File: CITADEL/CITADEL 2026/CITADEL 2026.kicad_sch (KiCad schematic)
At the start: 33 parts, among them J1 Vibration Motor, J2 Linear Actuator, U3 TJA1051T-3

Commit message: Updated Schematic
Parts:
- removed A1, A2: Pololu_Breakout_DRV8825, Module:Pololu_Breakout-16_15.2x20.3mm, symbol Driver_Motor:Pololu_Breakout_DRV8825
- added J18: CAN BUS, Connector_AMASS:AMASS_XT30U-F_1x02_P5.0mm_Vertical, symbol Connector:Conn_01x02_Pin
- added J19: Battery Connections, Connector_AMASS:AMASS_XT60-M_1x02_P7.20mm_Vertical, symbol Connector:Conn_01x02_Pin
- added J3: LED Strip, Connector_JST:JST_EH_B3B-EH-A_1x03_P2.50mm_Vertical, symbol Connector:Conn_01x03_Pin
- added J4: Spark Max, Connector_JST:JST_EH_B2B-EH-A_1x02_P2.50mm_Vertical, symbol Connector:Conn_01x02_Pin
- added P1: PS1, Citadel:D24V15OF5, symbol Citadel-altium-import:root_2_Pololu_5V,_15A_Step-Down_Voltage_Regulator_D24V150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
- added P2: PS2, Citadel:D24V15OF5, symbol Citadel-altium-import:root_0_Pololu_12V,_15A_Step-Down_Voltage_Regulator_D24V15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
- added Q7: SSM3K329R_LF, Citadel:SSM3K329_LF, symbol Citadel-altium-import:root_0_SSM3K329R_LF
- added U1: VNH7070ASTR, Jayse_Footprints:SO_0ASTR_STM, symbol 2026-01-09_23-32-14:VNH7070ASTR
- MG90S1, MG90S2, MG90S3, MG90S4, MG90S5, MG90S6, MG90S7, MG90S8, MG90S9: footprint (none) -> Connector_Molex:Molex_Mini-Fit_Jr_5566-04A_2x02_P4.20mm_Vertical
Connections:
- net Vibration_Motor_1 is gone; now on net +12V: J1.2 (Pin_2)
- net +12V: now also J3.1 (Pin_1), P2.VOUT, P2.VOUT_1 (VOUT), P2.VOUT_2 (VOUT)
- net +5V: now also P1.VOUT, P1.VOUT_1 (VOUT), P1.VOUT_2 (VOUT)
- net +BATT: now also J19.2 (Pin_2), P1.VIN, P1.VIN_1 (VIN), P1.VIN_2 (VIN), P2.VIN, P2.VIN_1 (VIN), P2.VIN_2 (VIN), U1.12 (VCC), U1.4 (VCC), U1.5 (VCC)
- net CIT_CAN+: now also J18.2 (Pin_2)
- net CIT_CAN-: now also J18.1 (Pin_1)
- net CRX_ESP: now also U2.12 (GPIO12/A15); no longer U2.11 (GPIO14/A16)
- net GND: now also J19.1 (Pin_1), J3.3 (Pin_3), J4.2 (Pin_2), P1.GND, P1.GND1 (GND), P1.GND2 (GND), P1.GND3 (GND), P1.GND4 (GND), P1.GND5 (GND), P1.GND6 (GND), P1.GND7 (GND), P2.GND, P2.GND1 (GND), P2.GND2 (GND), P2.GND3 (GND), P2.GND4 (GND), P2.GND5 (GND), P2.GND6 (GND), P2.GND7 (GND), Q7.2, U1.1 (GNDA), U1.16 (GNDA), U1.8 (GNDB), U1.9 (GNDB)
- net MG90S1: now also U2.30 (GPIO23/MOSI); no longer U2.9 (GPIO26/A19)
- net MG90S2: now also U2.29 (GPIO22/SCL); no longer U2.12 (GPIO12/A15)
- net MG90S3: now also U2.28 (GPIO1/TX0); no longer U2.30 (GPIO23/MOSI)
- net MG90S4: now also U2.27 (GPIO3/RX0); no longer U2.29 (GPIO22/SCL)
- net MG90S5: now also U2.26 (GPIO21/SDA); no longer U2.28 (GPIO1/TX0)
- net MG90S6: now also U2.25 (GPIO19/MISO); no longer U2.27 (GPIO3/RX0)
- net MG90S7: now also U2.24 (GPIO18/SCK); no longer U2.26 (GPIO21/SDA)
- net MG90S8: now also U2.23 (GPIO05/CS); no longer U2.25 (GPIO19/MISO)
- net MG90S9: now also U2.22 (GPIO17/TX2); no longer U2.24 (GPIO18/SCK)
- net DIR renamed Actuator_INA
- net Actuator_INA: now also U1.3 (INA)
- net Linear_Actuator_1 renamed Lin_Actuator_A
- net Lin_Actuator_A: now also U1.15 (OUTA), U1.2 (OUTA)
- net Linear_Actuator_2 renamed Lin_Actuator_B
- net Lin_Actuator_B: now also U1.10 (OUTB), U1.7 (OUTB)
- net Linear_Actuator_STEP renamed VibMotorSignal
- net VibMotorSignal: now also Q7.1
- net Step_Motor_Enable renamed LED_Strip
- net LED_Strip: now also J3.2 (Pin_2)
- net Vibration_Motor_2 renamed VibMotorMOS
- net VibMotorMOS: now also Q7.3
- net Vibration_Motor_STEP renamed Actuator_INB
- net Actuator_INB: now also U1.6 (INB)
- new net Actuator_PWM: U1.11 (PWM), U2.9 (GPIO26/A19)
- new net Spark_Max_PWM: J4.1 (Pin_1), U2.11 (GPIO14/A16)
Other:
- note added: "CAN Transceiver"
- note added: "Communication and Power"
- note added: "LED Strip"
- note added: "MCU"
- note added: "Power Regulators"
- moved on the sheet: C1, C2, C3, D4, J1, J2, JP1, MG90S1, MG90S2, MG90S3, MG90S4, MG90S5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

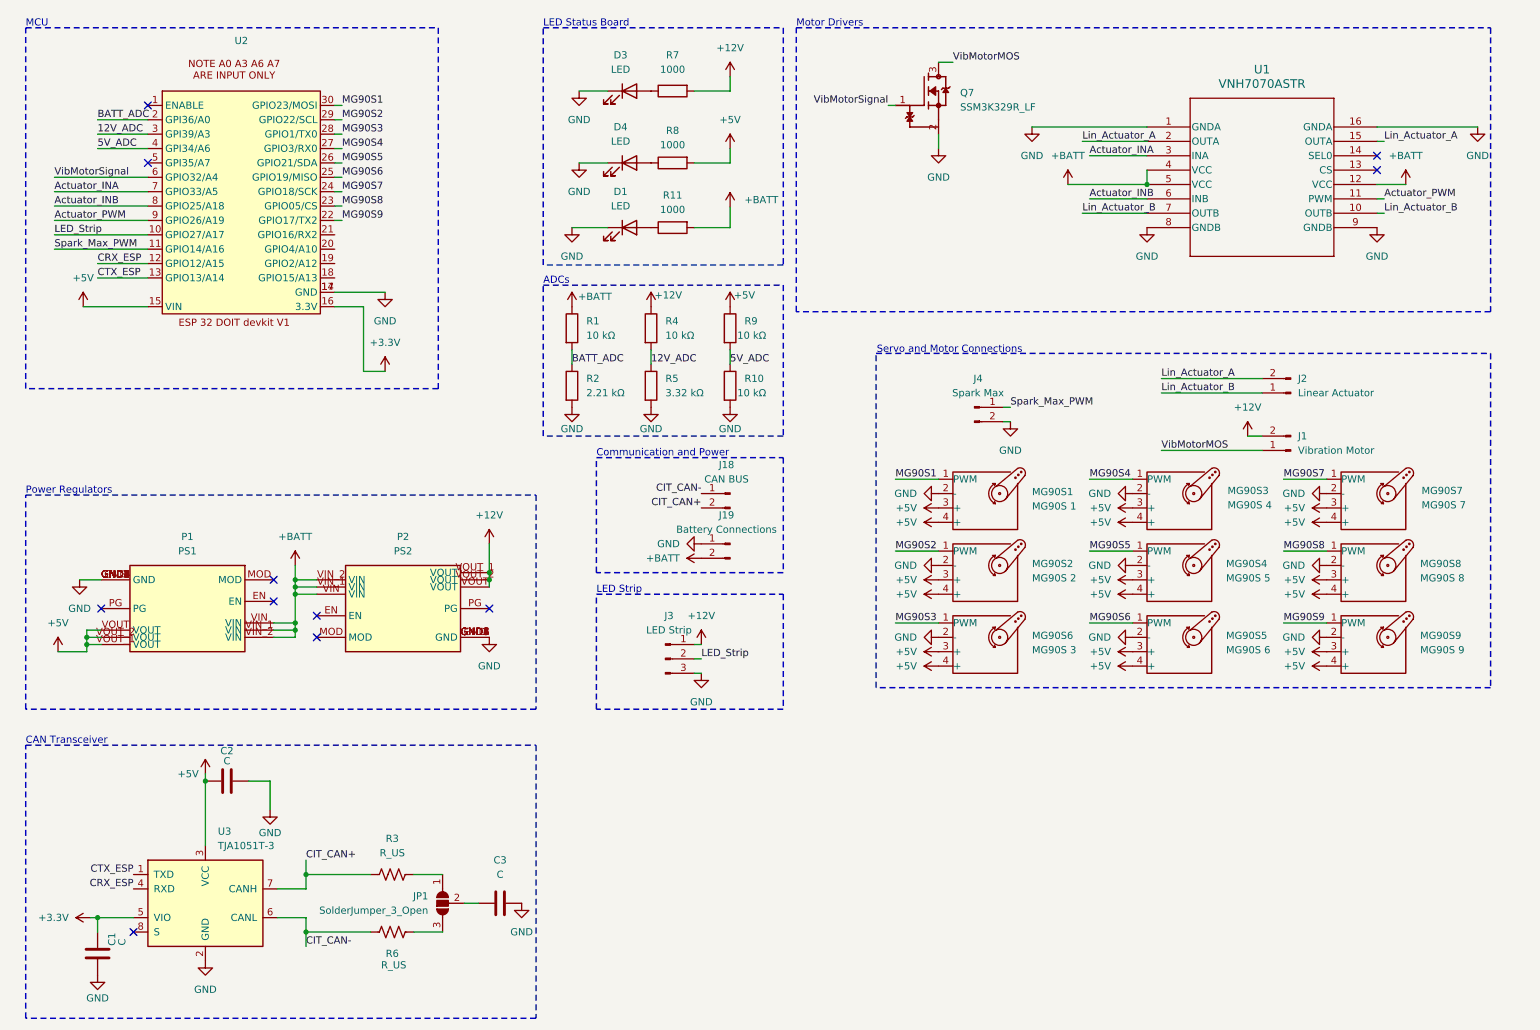
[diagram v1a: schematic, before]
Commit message: Updated Schematic
Changed MCU, added additional connectors
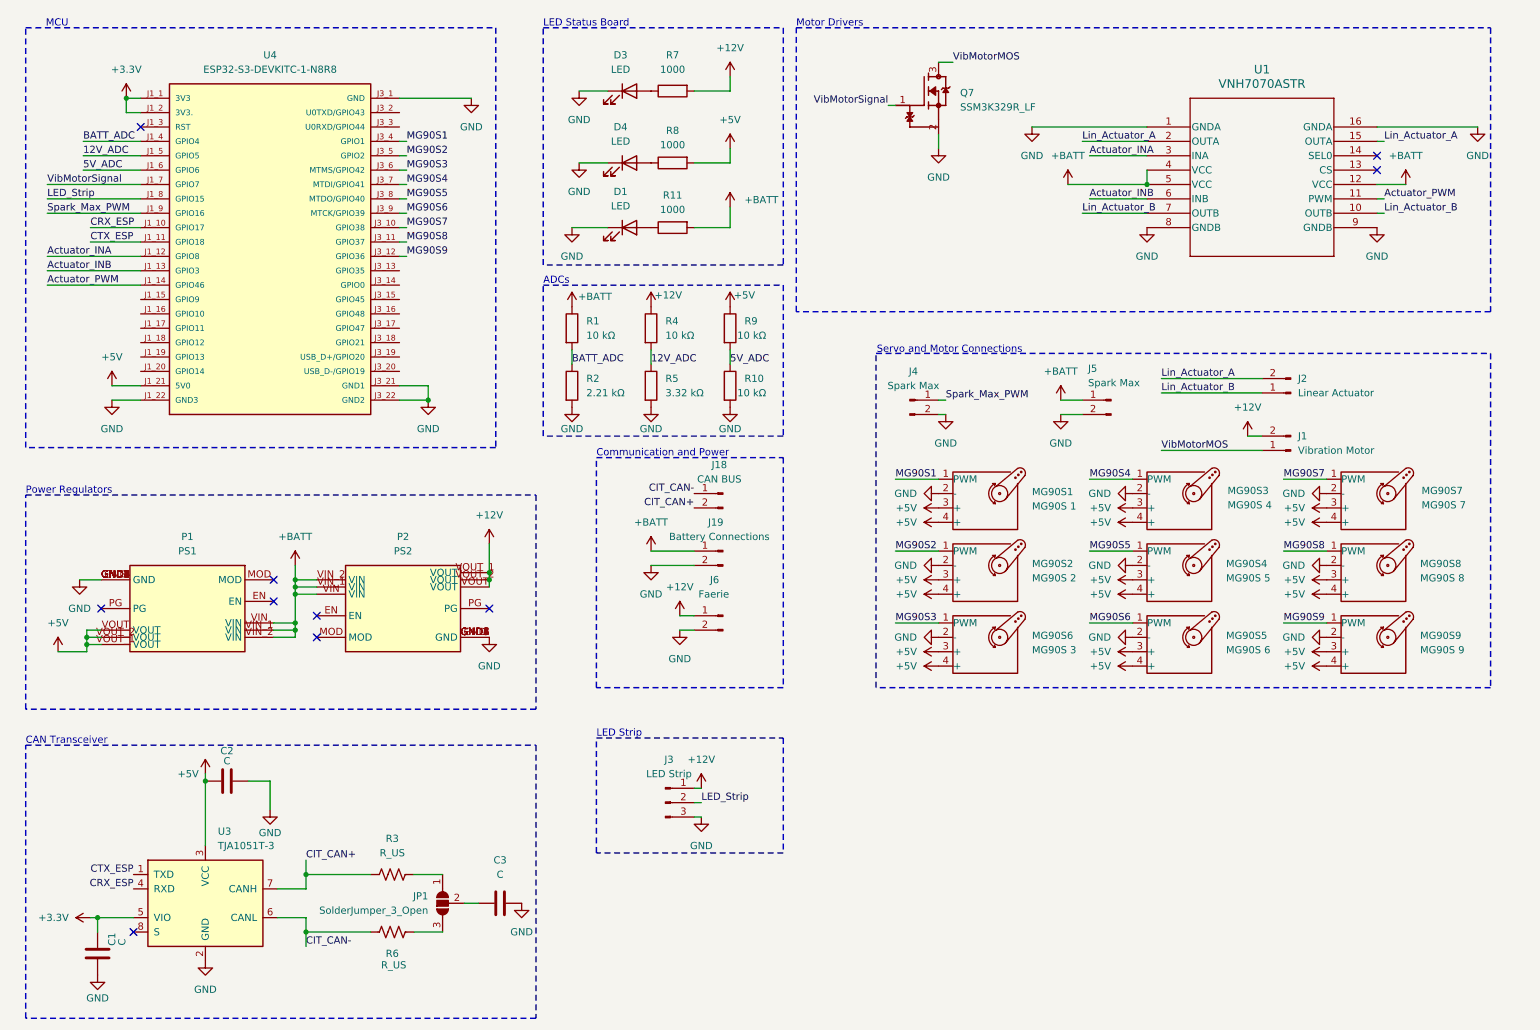
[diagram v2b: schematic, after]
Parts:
- removed U2: ~, Citadel:esp32_devkit_v1, symbol ESP 32 DOIT devkit V1:ESP32_DOIT_devkit_V1
- added J5: Spark Max, Connector_AMASS:AMASS_XT30U-F_1x02_P5.0mm_Vertical, symbol Connector:Conn_01x02_Pin
- added J6: Faerie, Connector_AMASS:AMASS_XT30U-F_1x02_P5.0mm_Vertical, symbol Connector:Conn_01x02_Pin
- added U4: ESP32-S3-DEVKITC-1-N8R8, Jayse_Footprints:ESP32-S3-DEVKITC-1-N8R8, symbol ESP32-S3-DEVKITC-1-N8R8:ESP32-S3-DEVKITC-1-N8R8
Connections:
- net +12V: now also J6.1 (Pin_1)
- net +3.3V: now also U4.J1_1 (3V3), U4.J1_2 (3V3.)
- net +5V: now also U4.J1_21 (5V0)
- net +BATT: now also J19.1 (Pin_1), J5.1 (Pin_1); no longer J19.2 (Pin_2)
- net 12V_ADC: now also U4.J1_5 (GPIO5)
- net 5V_ADC: now also U4.J1_6 (GPIO6)
- net Actuator_INA: now also U4.J1_12 (GPIO8)
- net Actuator_INB: now also U4.J1_13 (GPIO3)
- net Actuator_PWM: now also U4.J1_14 (GPIO46)
- net BATT_ADC: now also U4.J1_4 (GPIO4)
- net CRX_ESP: now also U4.J1_10 (GPIO17)
- net CTX_ESP: now also U4.J1_11 (GPIO18)
- net GND: now also J19.2 (Pin_2), J5.2 (Pin_2), J6.2 (Pin_2), U4.J1_22 (GND3), U4.J3_1 (GND), U4.J3_21 (GND1), U4.J3_22 (GND2); no longer J19.1 (Pin_1)
- net LED_Strip: now also U4.J1_8 (GPIO15)
- net MG90S1: now also U4.J3_4 (GPIO1)
- net MG90S2: now also U4.J3_5 (GPIO2)
- net MG90S3: now also U4.J3_6 (MTMS/GPIO42)
- net MG90S4: now also U4.J3_7 (MTDI/GPIO41)
- net MG90S5: now also U4.J3_8 (MTDO/GPIO40)
- net MG90S6: now also U4.J3_9 (MTCK/GPIO39)
- net MG90S7: now also U4.J3_10 (GPIO38)
- net MG90S8: now also U4.J3_11 (GPIO37)
- net MG90S9: now also U4.J3_12 (GPIO36)
- net Spark_Max_PWM: now also U4.J1_9 (GPIO16)
- net VibMotorSignal: now also U4.J1_7 (GPIO7)
- no-connect marks 11 -> 10
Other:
- moved on the sheet: J18, J19, J3, J4

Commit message: Updated Schematic
Changed motor drivers and connectors
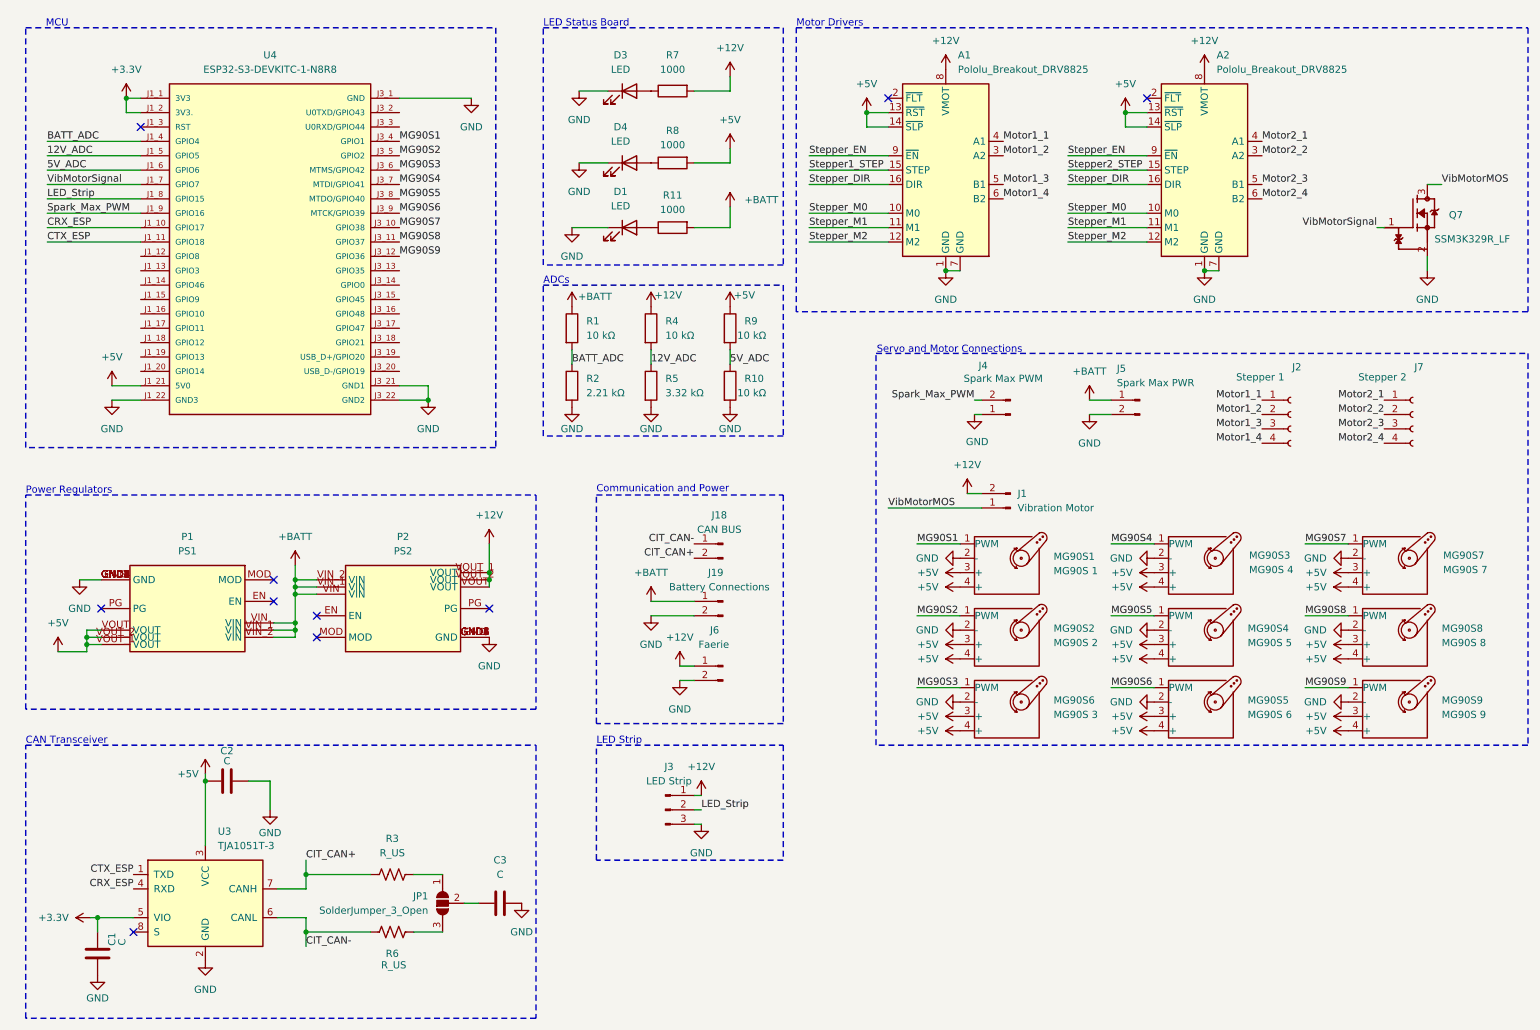
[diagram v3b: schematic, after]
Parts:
- removed J2: Linear Actuator, Connector_Molex:Molex_Mini-Fit_Jr_5566-02A_2x01_P4.20mm_Vertical, symbol Connector:Conn_01x02_Pin
- removed U1: VNH7070ASTR, Jayse_Footprints:SO_0ASTR_STM, symbol 2026-01-09_23-32-14:VNH7070ASTR
- added A1, A2: Pololu_Breakout_DRV8825, Module:Pololu_Breakout-16_15.2x20.3mm, symbol Driver_Motor:Pololu_Breakout_DRV8825
- added J2: Stepper 1, Connector_Molex:Molex_Mini-Fit_Jr_5566-04A_2x02_P4.20mm_Vertical, symbol Connector:Conn_01x04_Socket
- added J7: Stepper 2, Connector_Molex:Molex_Mini-Fit_Jr_5566-04A_2x02_P4.20mm_Vertical, symbol Connector:Conn_01x04_Socket
- J4: value Spark Max -> Spark Max PWM
- J5: value Spark Max -> Spark Max PWR
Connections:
- net +12V: now also A1.8 (VMOT), A2.8 (VMOT)
- net +5V: now also A1.13 (~{RST}), A1.14 (~{SLP}), A2.13 (~{RST}), A2.14 (~{SLP})
- net GND: now also J4.1 (Pin_1), A1.1 (GND), A1.7 (GND), A2.1 (GND), A2.7 (GND); no longer J4.2 (Pin_2)
- net Spark_Max_PWM: now also J4.2 (Pin_2); no longer J4.1 (Pin_1)
- net Actuator_INA: no longer names the net of U4.J1_12 (GPIO8)
- net Actuator_INB: no longer names the net of U4.J1_13 (GPIO3)
- net Actuator_PWM: no longer names the net of U4.J1_14 (GPIO46)
- new net Motor1_1: A1.4 (A1), J2.1 (Pin_1)
- new net Motor1_2: A1.3 (A2), J2.2 (Pin_2)
- new net Motor1_3: A1.5 (B1), J2.3 (Pin_3)
- new net Motor1_4: A1.6 (B2), J2.4 (Pin_4)
- new net Motor2_1: A2.4 (A1), J7.1 (Pin_1)
- new net Motor2_2: A2.3 (A2), J7.2 (Pin_2)
- new net Motor2_3: A2.5 (B1), J7.3 (Pin_3)
- new net Motor2_4: A2.6 (B2), J7.4 (Pin_4)
- new net Stepper1_STEP: A1.15 (STEP)
- new net Stepper2_STEP: A2.15 (STEP)
- new net Stepper_DIR: A1.16 (DIR), A2.16 (DIR)
- new net Stepper_EN: A1.9 (~{EN}), A2.9 (~{EN})
- new net Stepper_M0: A1.10 (M0), A2.10 (M0)
- new net Stepper_M1: A1.11 (M1), A2.11 (M1)
- new net Stepper_M2: A1.12 (M2), A2.12 (M2)
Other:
- moved on the sheet: J1, J18, J19, J3, J4, J5, J6, MG90S1, MG90S2, MG90S3, MG90S4, MG90S5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

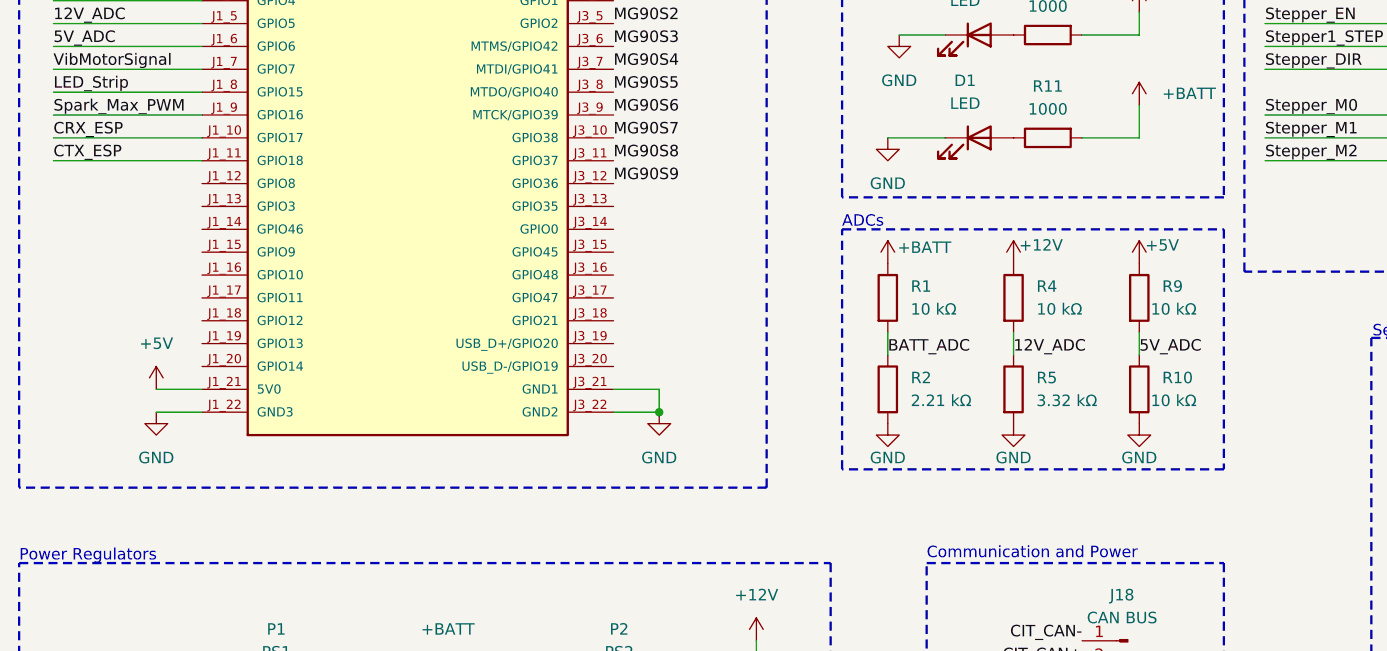
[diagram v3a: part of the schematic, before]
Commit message: Changed 5V buck from 15A to 11A
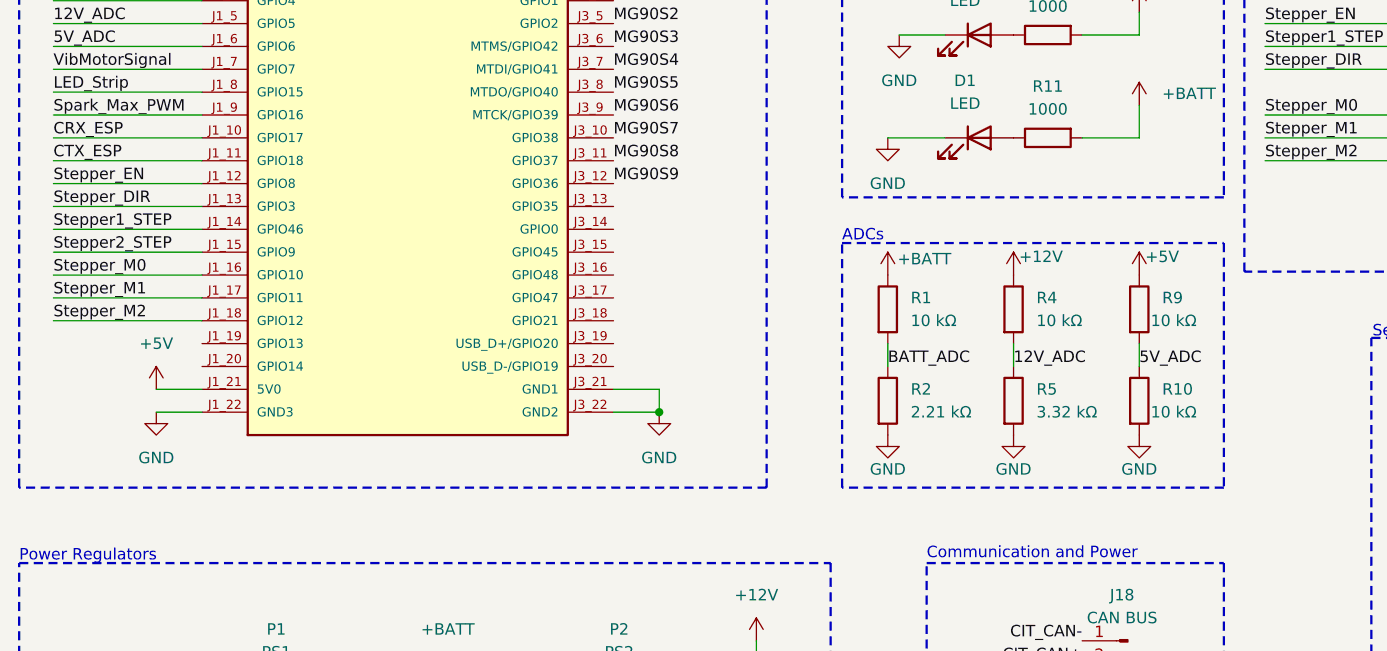
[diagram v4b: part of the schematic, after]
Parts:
- P1: symbol Citadel-altium-import:root_2_Pololu_5V,_15A_Step-Down_Voltage_Regulator_D24V150F5 -> Citadel-altium-import:root_2_Pololu_5V,_11A_Step-Down_Voltage_Regulator_D42V110F5
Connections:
- net Stepper1_STEP: now also U4.J1_14 (GPIO46)
- net Stepper2_STEP: now also U4.J1_15 (GPIO9)
- net Stepper_DIR: now also U4.J1_13 (GPIO3)
- net Stepper_EN: now also U4.J1_12 (GPIO8)
- net Stepper_M0: now also U4.J1_16 (GPIO10)
- net Stepper_M1: now also U4.J1_17 (GPIO11)
- net Stepper_M2: now also U4.J1_18 (GPIO12)
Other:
- moved on the sheet: R1, R10, R2, R4, R5, R9
